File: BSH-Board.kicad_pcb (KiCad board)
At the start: 2 copper layers, 20 x 30 mm, 70 parts, among them J1 667101210103, J2 MICRO QTZB5.0, SW1 TS-3025-B-C-B, SW2 TS-3025-B-C-B, U1 ESP32-C6-MINI-1-N4, U2 AP63203WU, U3 NCP715SQ50T2G, U4 LSF0102DQER

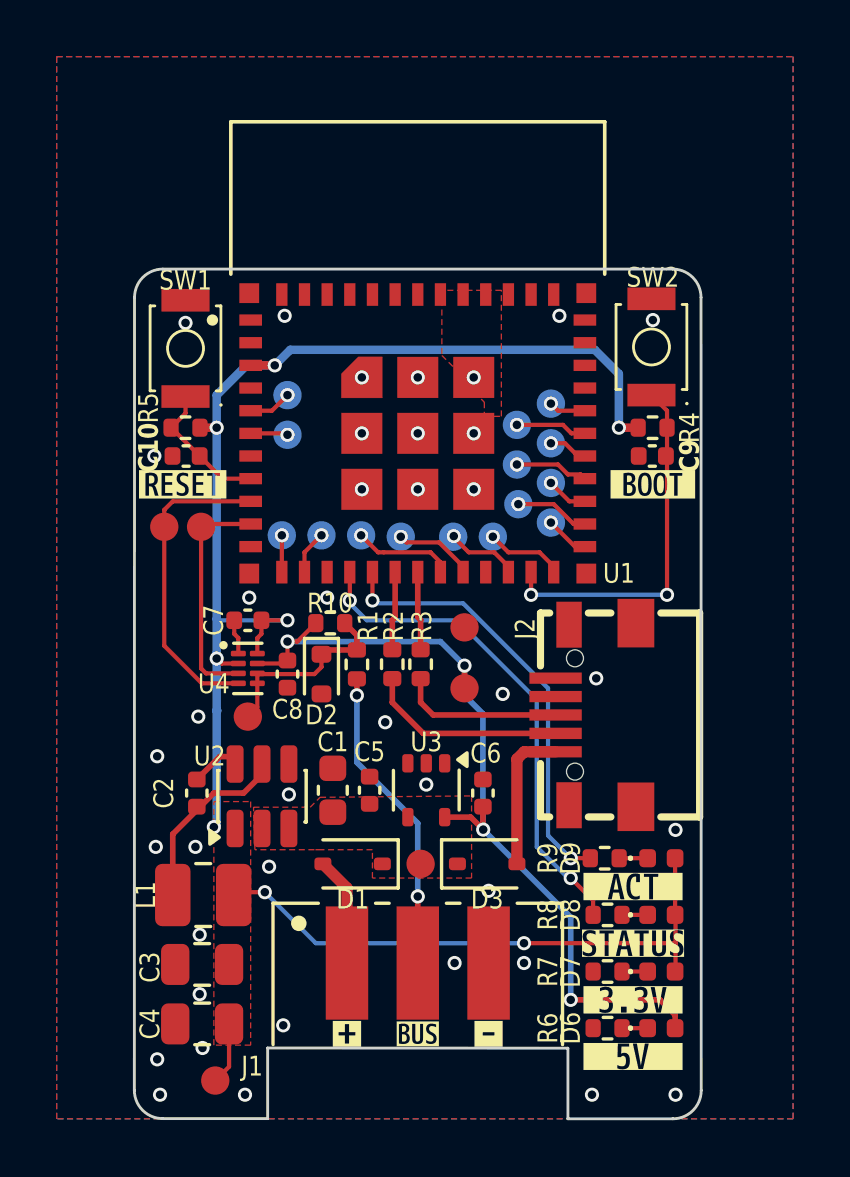
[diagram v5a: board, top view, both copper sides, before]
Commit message: Using 74LVC Logic, get rid of LDO for 5V
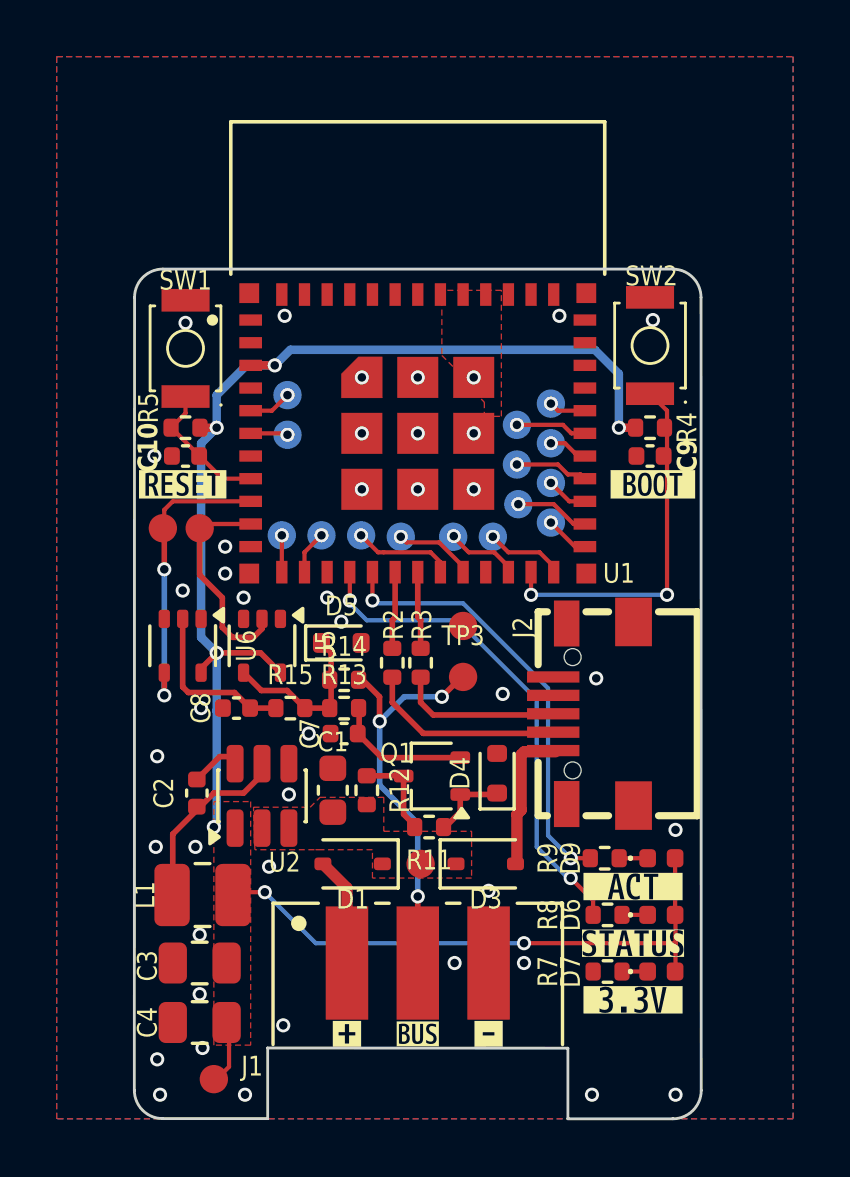
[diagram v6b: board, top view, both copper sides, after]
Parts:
- removed C5, C6: 1uF, Capacitor_SMD:C_0402_1005Metric
- removed D2: BZX584C5V6, Diode_SMD:D_SOD-523
- removed D8: LED_Y, LED_SMD:LED_0402_1005Metric
- removed R1: 330, Resistor_SMD:R_0402_1005Metric
- removed R10: 10k, Resistor_SMD:R_0402_1005Metric
- removed R6: 510, Resistor_SMD:R_0402_1005Metric
- removed TP7: TestPoint, Testpoints:TestPoint_Pad_D1.0mm
- removed U3: NCP715SQ50T2G, Package_TO_SOT_SMD:SOT-353_SC-70-5
- removed U4: LSF0102DQER, Package_SON:X2SON-8_1.4x1mm_P0.35mm
- removed kibuzzard-695C20B7: G***, kibuzzard-695C20B7
- added D4: BZX584C5V6, Diode_SMD:D_SOD-523, F.Cu at (124.8, 78.8)
- added D5: BZX584C5V6, Diode_SMD:D_SOD-523, F.Cu at (119.3, 74.2)
- added Q1: MMST3904, Package_TO_SOT_SMD:SOT-323_SC-70, F.Cu at (122.5, 78.9)
- added R11: 100K, Resistor_SMD:R_0402_1005Metric, F.Cu at (122.4, 80.7)
- added R12: 1K, Resistor_SMD:R_0402_1005Metric, F.Cu at (120.2, 79.4)
- added R13: 10k, Resistor_SMD:R_0402_1005Metric, F.Cu at (119.4, 76.5)
- added R14: 100, Resistor_SMD:R_0402_1005Metric, F.Cu at (119.4, 75.5)
- added R15: 1K, Resistor_SMD:R_0402_1005Metric, F.Cu at (117.5, 76.5)
- added U5: 74LVC1G07, Package_TO_SOT_SMD:SOT-353_SC-70-5, F.Cu at (116.5, 74.3)
- added U6: 74LVC1G17, Package_TO_SOT_SMD:SOT-353_SC-70-5, F.Cu at (113.7, 74.3)
- C8: value 100nF -> 1nF
- moved TP3 7.73 mm to (123.6, 75.4)
- moved C7 5.25 mm to (119.4, 77.4)
- moved D6 4.00 mm to (130.6, 83.8)
- moved C8 2.16 mm to (115.6, 76.5), turned to 0 degrees
- moved C4 0.10 mm to (114.3, 87.6)
- moved C3 0.10 mm to (114.3, 85.5)
- moved J2 0.09 mm to (128.2, 76.7)
- moved R4 0.09 mm to (130.2, 66.6)
- moved C9 0.08 mm to (130.2, 67.6)
- moved TP4 0.07 mm to (123.6, 73.6)
- moved SW2 0.07 mm to (130.2, 63.7)
- moved TP1 0.07 mm to (114.3, 70.2)
- moved TP2 0.07 mm to (113.0, 70.2)
- moved TP6 0.07 mm to (114.8, 89.6)
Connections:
- C7 pad 2: +3.3V -> Net-(Q1-E)
- C8 pad 2: +5V -> Net-(C8-Pad2)
- D6 pad 2: +5V -> +3.3V
- J1 pad A2: /DBUS -> Net-(J1-PadA2)
- R8 pad 2: Net-(D8-K) -> Net-(D6-K)
- TP1 pad 1: DBUS-RX -> DBUS-TX
- TP2 pad 1: DBUS-TX -> DBUS-RX
- TP3 pad 1: Net-(D2-K) -> Net-(J1-PadA2)
- U1 pad 10: DBUS-RX -> DBUS-TX
- U1 pad 9: DBUS-TX -> DBUS-RX
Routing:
- net +5V: track 30.5 -> 0.00 mm, vias 4 -> 0
- net Net-(J1-PadA2): track 0.00 -> 14.5 mm, vias 0 -> 3
- net /DBUS: track 10.9 -> 0.00 mm, vias 2 -> 0
- net Net-(D2-K): track 6.93 -> 0.00 mm
- net Net-(C8-Pad2): track 0.00 -> 6.00 mm
- net Net-(D5-K): track 0.00 -> 5.93 mm
- net Net-(Q1-E): track 0.00 -> 4.86 mm
- net DBUS-TX: track 11.1 -> 7.66 mm
- net Net-(Q1-C): track 0.00 -> 3.24 mm
- net Net-(D4-K): track 0.00 -> 2.72 mm
- net DBUS-RX: track 8.20 -> 10.4 mm, vias 0 -> 2
- net +3.3V: track 62.6 -> 61.1 mm, vias 8 -> 7
- net GND: track 1.24 -> 0.00 mm, vias 39 -> 42
- net Net-(D8-K): track 0.91 -> 0.00 mm

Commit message: Finished layout
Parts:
- moved R5 3.20 mm to (114.4, 77.3), turned to 90 degrees
- moved D4 2.50 mm to (130.6, 88.3)
- moved R6 2.50 mm to (128.7, 88.3)
- moved kibuzzard-695C20B0 2.50 mm to (129.6, 89.3)
- moved C2 2.34 mm to (113.4, 77.3), turned to 90 degrees
- moved D5 1.50 mm to (130.6, 85.3)
- moved R7 1.50 mm to (128.7, 85.3)
- moved kibuzzard-695C20AA 1.50 mm to (129.6, 86.3)
- moved D6 0.50 mm to (130.6, 82.3)
- moved R8 0.50 mm to (128.6, 82.3)
- moved kibuzzard-695C20DE 0.50 mm to (129.6, 83.3)
- moved C3 0.40 mm to (119.0, 79.8)
- moved D1 0.30 mm to (119.7, 82.3)
- moved D7 0.30 mm to (124.4, 82.3)
- moved C4 0.14 mm to (114.3, 79.6)
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- renumbered C7 to C1, C8 to C2, C1 to C3, C2 to C4, C3 to C5, C4 to C6, C9 to C7, C10 to C8, D5 to D2, D4 to D3, D7 to D4, D6 to D5, D9 to D6, D3 to D7, R14 to R1, R3 to R10, R4 to R11, R5 to R12, R12 to R2, R11 to R3, R13 to R4, R15 to R5, R7 to R6, R8 to R7, R9 to R8, R2 to R9, SW2 to SW1, SW1 to SW2, TP4 to TP1, TP11 to TP10, TP12 to TP11, TP21 to TP12, TP22 to TP13, TP13 to TP14, TP14 to TP15, TP15 to TP16, TP16 to TP17, TP17 to TP18, TP18 to TP19, TP3 to TP2, TP19 to TP20, TP20 to TP21, TP1 to TP3, TP2 to TP4, TP8 to TP7, TP9 to TP8, TP10 to TP9, U5 to U1, U6 to U2, U2 to U3, U1 to U4
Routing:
- net +3.3V: track 61.1 -> 64.6 mm
- net Net-(D2-K): track 5.93 -> 8.12 mm
- net DBUS-RX: track 10.4 -> 8.84 mm
- net STATUS: track 17.6 -> 19.2 mm
- net Net-(C2-Pad2): track 6.00 -> 5.05 mm
- net GND: vias 42 -> 48

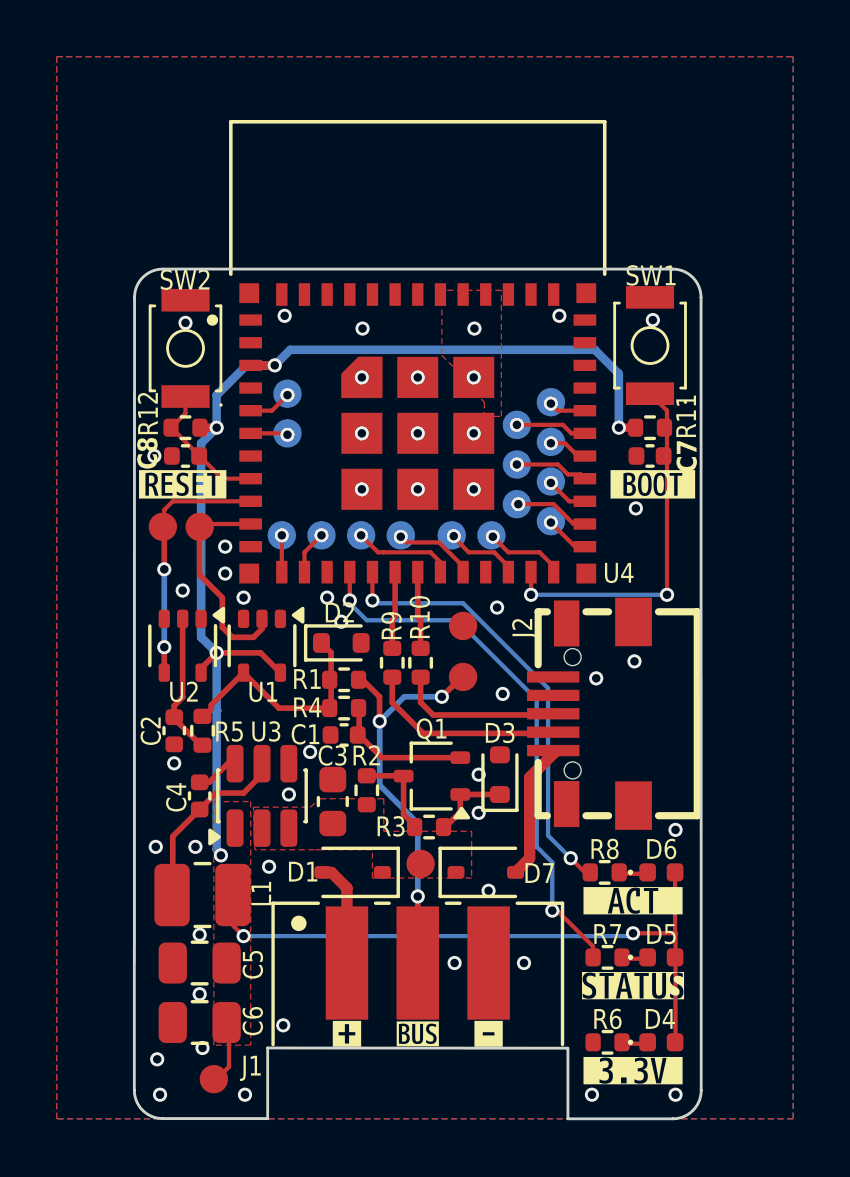
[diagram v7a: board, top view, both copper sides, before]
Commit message: Extended board to reach under the antenna
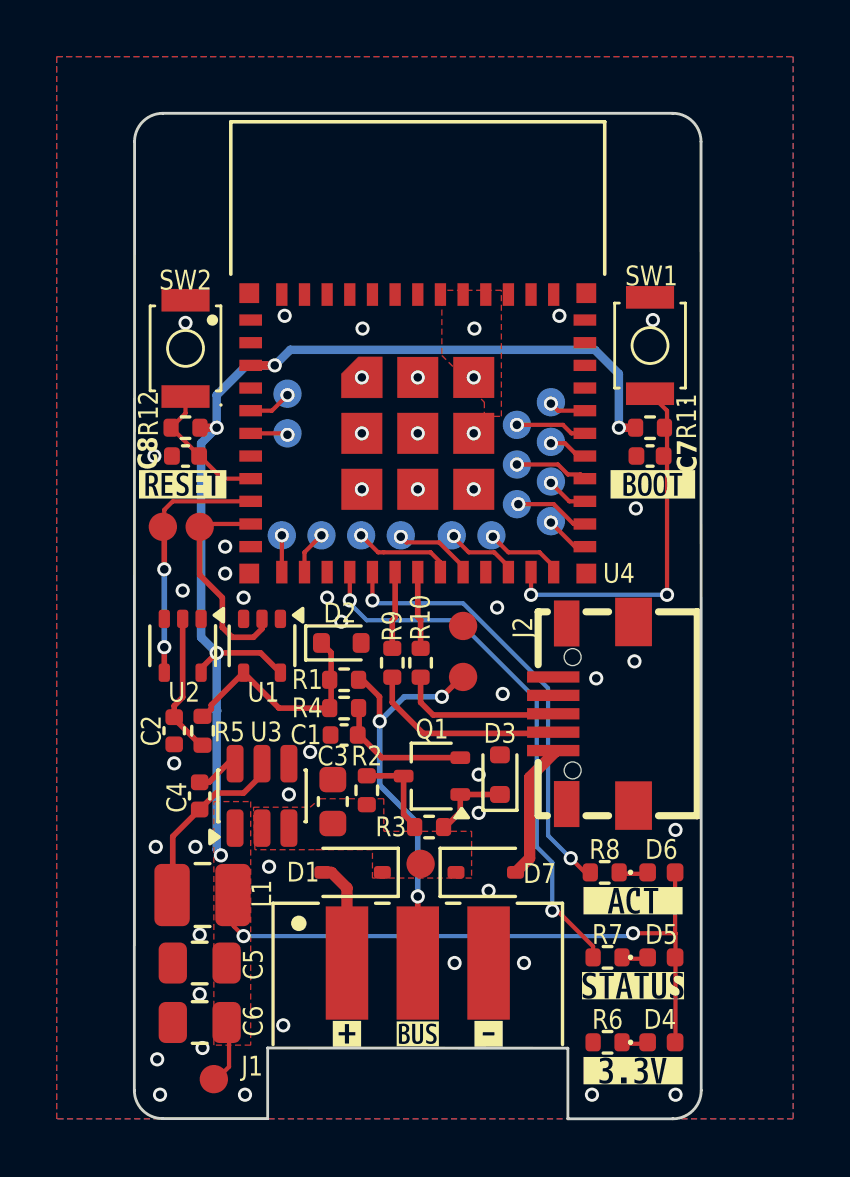
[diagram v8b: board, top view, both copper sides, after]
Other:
- board size 20 x 30 mm -> 20 x 35.5 mm
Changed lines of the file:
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@@
 		(title "BSH Board")
 		(date "2026-01-16")
-		(rev "1.0-RC2")
+		(rev "1.0")
 		(company "Bouni")
 	)
@@
 	)
 	(gr_line
-		(start 113 61)
-		(end 131 61)
+		(start 113 55.5)
+		(end 131 55.5)
 		(stroke
 			(width 0.1)
@@
 	)
 	(gr_arc
-		(start 131 61)
-		(mid 131.707107 61.292893)
-		(end 132 62)
+		(start 131 55.5)
+		(mid 131.707107 55.792893)
+		(end 132 56.5)
 		(stroke
 			(width 0.1)
@@
 	)
 	(gr_line
-		(start 132.000245 62)
+		(start 132 56.5)
 		(end 132.007107 90)
 		(stroke
@@
 	(gr_line
 		(start 111.992893 89.992893)
-		(end 111.999755 62)
+		(end 112.001103 56.5)
 		(stroke
 			(width 0.1)
@@
 	)
 	(gr_arc
-		(start 112 62)
-		(mid 112.292893 61.292893)
-		(end 113 61)
+		(start 112 56.5)
+		(mid 112.292893 55.792893)
+		(end 113 55.5)
 		(stroke
 			(width 0.1)
@@
 		(layer "User.1")
 		(pts
+			(xy 132 61) (xy 132 55.5)
+		)
+		(height 6.2)
+		(orientation 1)
+		(format
+			(prefix "")
+			(suffix "")
+			(units 3)
+			(units_format 0)
+			(precision 4)
+			(suppress_zeroes yes)
+		)
+		(style
+			(thickness 0.1)
+			(arrow_length 1.27)
+			(text_position_mode 0)
+			(arrow_direction outward)
+			(extension_height 0.58642)
+			(extension_offset 0.5)
+			(keep_text_aligned yes)
+		)
+		(gr_text "5.5"
+			(at 137.05 58.25 90)
+			(layer "User.1")
+			(effects
+				(font
+					(size 1 1)
+					(thickness 0.15)
+				)
+			)
+		)
+	)
+	(dimension
+		(type orthogonal)
+		(layer "User.1")
+		(pts
 			(xy 112 60) (xy 132 60)
 		)
@@
 			)
 		)
+	)
+	(zone
+		(net 0)
+		(net_name "")
+		(layers "F.Cu" "B.Cu" "User.1")
+		(name "Antenna-Keepout")
+		(hatch edge 0.5)
+		(connect_pads
+			(clearance 0)
+		)
+		(min_thickness 0.25)
+		(filled_areas_thickness no)
+		(keepout
+			(tracks not_allowed)
+			(vias not_allowed)
+			(pads not_allowed)
+			(copperpour not_allowed)
+			(footprints allowed)
+		)
+		(placement
+			(enabled no)
+			(sheetname "")
+		)
+		(fill
+			(thermal_gap 0.5)
+			(thermal_bridge_width 0.5)
+		)
+		(polygon
+			(pts
+				(xy 112 55.5) (xy 132 55.5) (xy 132 61.25) (xy 112 61.25)
+			)
+		)
